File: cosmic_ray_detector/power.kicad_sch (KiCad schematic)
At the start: 16 parts, among them U2 TPS7A30, U3 TPS7A49

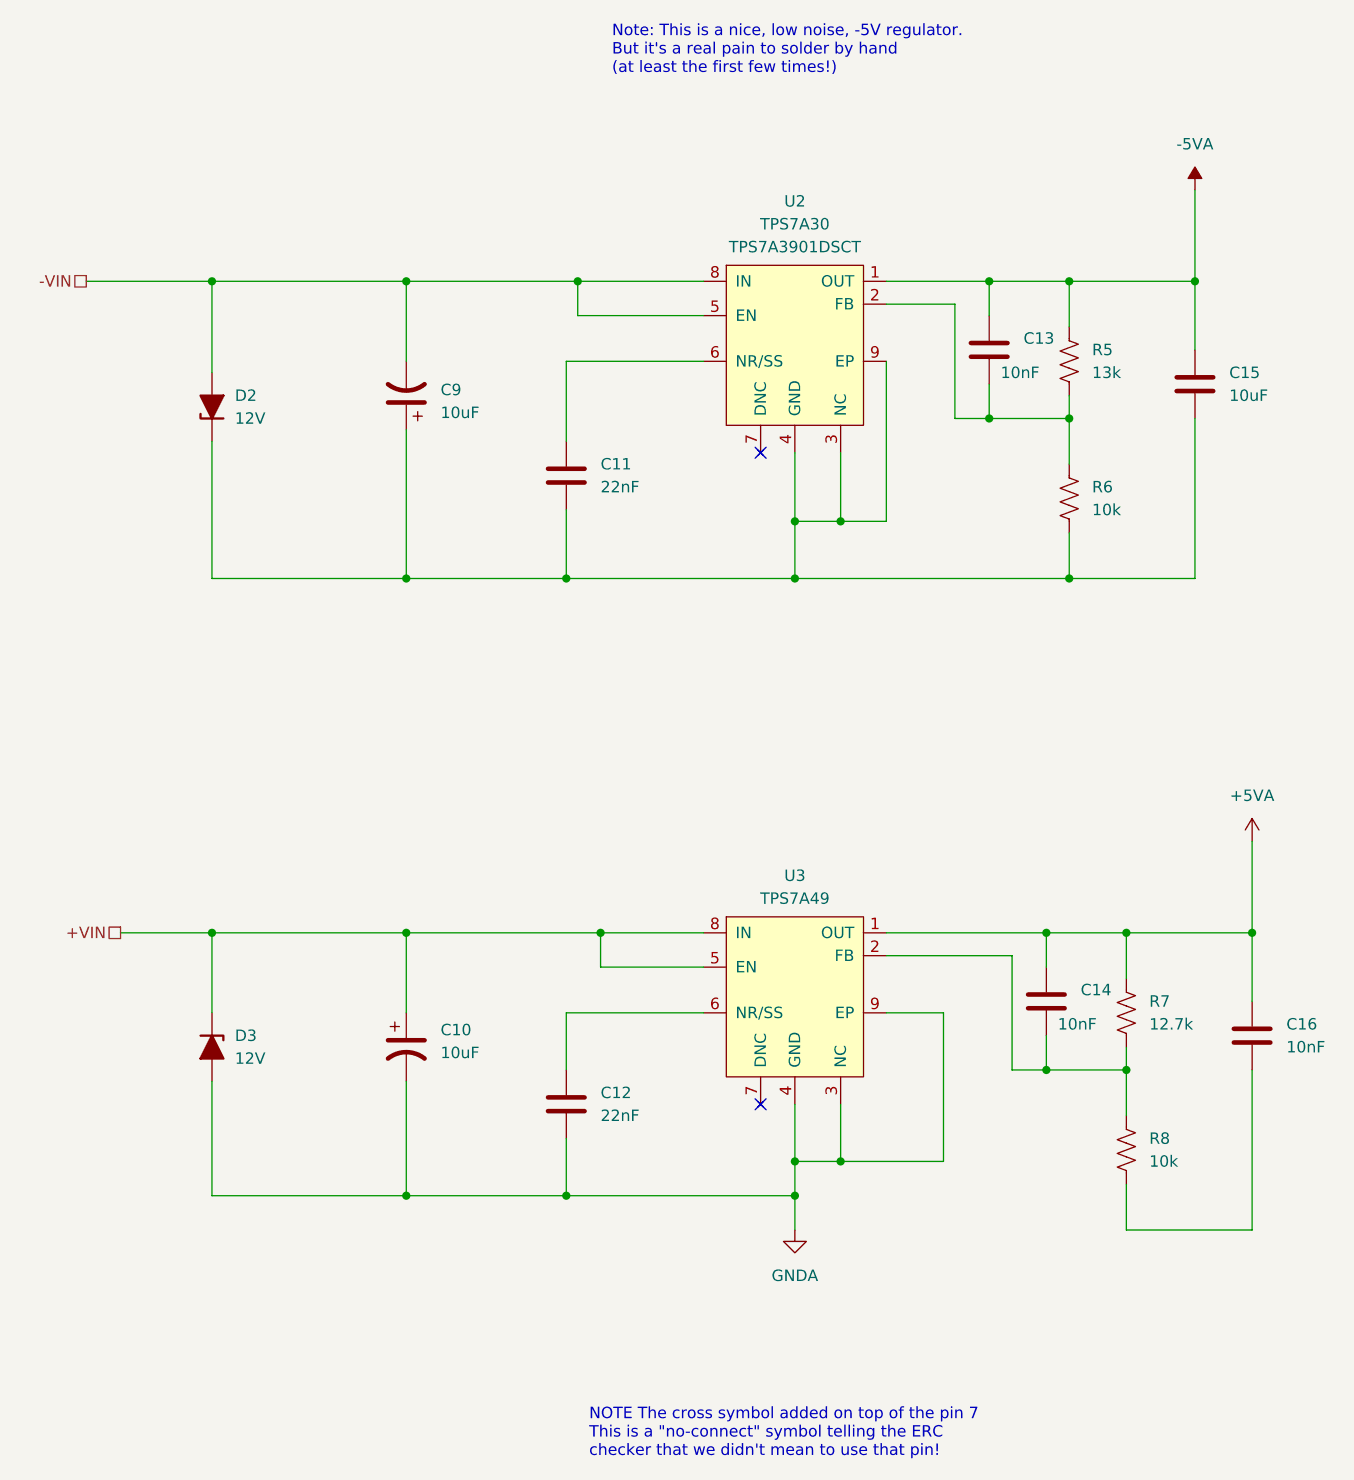
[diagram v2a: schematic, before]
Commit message: updated, now passes ERC
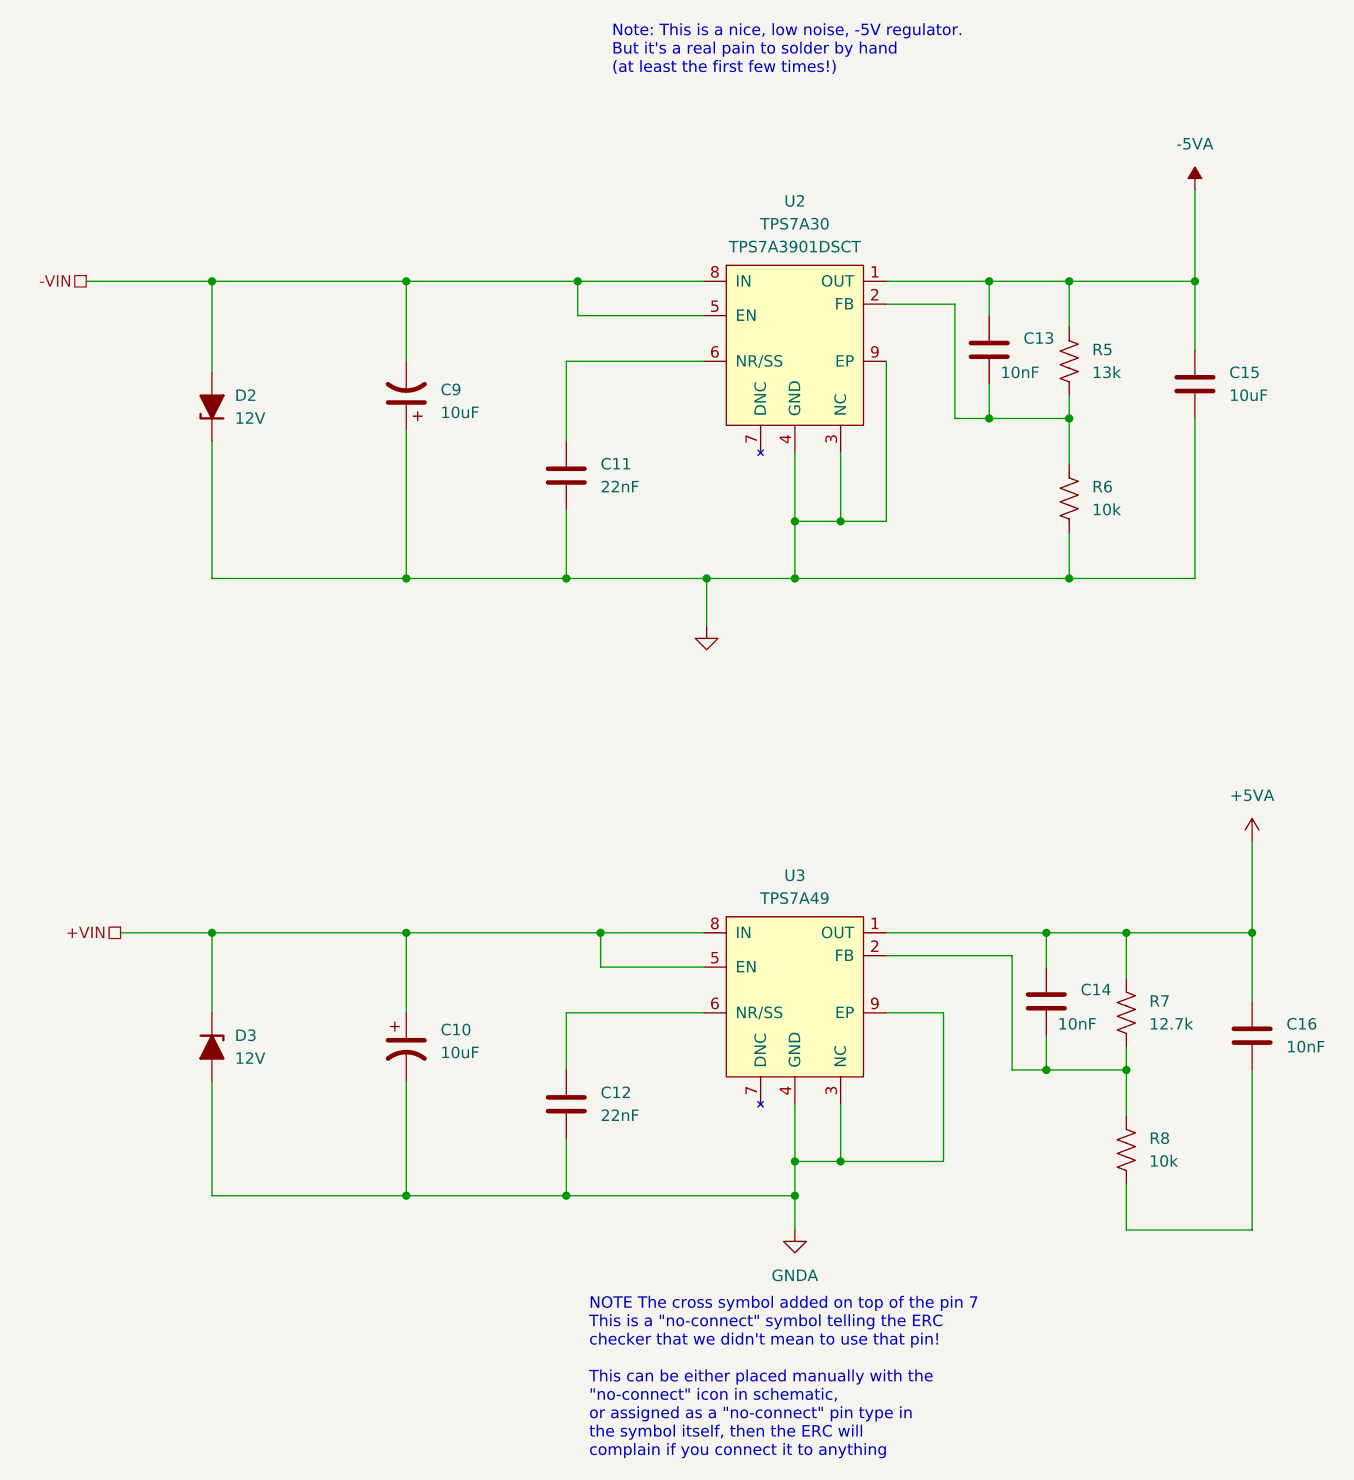
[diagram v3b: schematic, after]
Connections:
- net GNDA: now also C11.2, C15.2, C9.1, D2.1 (K), R6.2, U2.3 (NC), U2.4 (GND), U2.9 (EP)
- no-connect marks 2 -> 0
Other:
- note added: "NOTE The cross symbol added on top of the pin 7 This is a "no-connect" symbol telling the ERC checker that we didn't mean to use that pin! This can be either placed manually with the "no-connect" icon in schematic, or assigned as a "no-connect" pin type in the symbol itself, then the ERC will complain if you connect it to anything"
- note removed: "NOTE The cross symbol added on top of the pin 7 This is a "no-connect" symbol telling the ERC checker that we didn't mean to use that pin!"

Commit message: add more 3d parts symbols to library
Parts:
- U2, U3: footprint SPIRIT:MSOP-8-1EP_3x3mm_P0.65mm_EP1.73x1.85mm_ThermalVias -> (none)
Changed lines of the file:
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@@
     (property "Reference" "U2" (id 0) (at 125.73 43.18 0))
     (property "Value" "TPS7A30" (id 1) (at 125.73 45.72 0))
-    (property "Footprint" "SPIRIT:MSOP-8-1EP_3x3mm_P0.65mm_EP1.73x1.85mm_ThermalVias" (id 2) (at 125.73 54.61 0)
+    (property "Footprint" "" (id 2) (at 125.73 54.61 0)
       (effects (font (size 1.27 1.27)) hide)
     )
@@
     (property "Reference" "U3" (id 0) (at 125.73 118.11 0))
     (property "Value" "TPS7A49" (id 1) (at 125.73 120.65 0))
-    (property "Footprint" "SPIRIT:MSOP-8-1EP_3x3mm_P0.65mm_EP1.73x1.85mm_ThermalVias" (id 2) (at 125.73 127 0)
+    (property "Footprint" "" (id 2) (at 125.73 127 0)
       (effects (font (size 1.27 1.27)) hide)
     )

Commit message: many more footprints coming in
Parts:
- C10, C15, C9: value 10uF -> (none); Farnell (none) -> 1187014; MPN (none) -> MAL215375109E3; Manufacturer_Name (none) -> Vishay
- C11, C12: value 22nF -> (none)
- C13, C14, C16: value 10nF -> (none)
- D2, D3: value 12V -> (none); footprint Diode_SMD:D_SOD-123 -> (none); Manufacturer ONSEMI -> (none); Manufacturer_Name (none) -> ONSEMI
- R5: value 13k -> (none)
- R6, R8: value 10k -> (none)
- R7: value 12.7k -> (none)
- U2: value TPS7A30 -> (none); Farnell (none) -> 1855138; farnell 1855138 -> (none)
- U3: value TPS7A49 -> (none); Farnell (none) -> 1841881; farnell 1841881 -> (none)
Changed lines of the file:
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@@
       (effects (font (size 1.27 1.27)) (justify left))
     )
-    (property "Value" "10k" (id 1) (at 165.1 149.8599 0)
+    (property "Value" "" (id 1) (at 165.1 149.8599 0)
       (effects (font (size 1.27 1.27)) (justify left))
     )
@@
       (effects (font (size 1.27 1.27)) (justify left))
     )
-    (property "Value" "12.7k" (id 1) (at 165.1 134.6199 0)
+    (property "Value" "" (id 1) (at 165.1 134.6199 0)
       (effects (font (size 1.27 1.27)) (justify left))
     )
@@
       (effects (font (size 1.27 1.27)) (justify left))
     )
-    (property "Value" "10uF" (id 1) (at 86.36 137.7949 0)
+    (property "Value" "" (id 1) (at 86.36 137.7949 0)
       (effects (font (size 1.27 1.27)) (justify left))
     )
@@
       (effects (font (size 1.27 1.27)) hide)
     )
+    (property "Farnell" "1187014 " (id 4) (at 82.55 137.16 0)
+      (effects (font (size 1.27 1.27)) hide)
+    )
+    (property "MPN" "MAL215375109E3" (id 5) (at 82.55 137.16 0)
+      (effects (font (size 1.27 1.27)) hide)
+    )
+    (property "Manufacturer_Name" "Vishay" (id 6) (at 82.55 137.16 0)
+      (effects (font (size 1.27 1.27)) hide)
+    )
     (pin "1")
     (pin "2")
@@
       (effects (font (size 1.27 1.27)) (justify left))
     )
-    (property "Value" "10nF" (id 1) (at 180.34 137.1599 0)
+    (property "Value" "" (id 1) (at 180.34 137.1599 0)
       (effects (font (size 1.27 1.27)) (justify left))
     )
@@
       (effects (font (size 1.27 1.27)) (justify left))
     )
-    (property "Value" "13k" (id 1) (at 158.75 62.2299 0)
+    (property "Value" "" (id 1) (at 158.75 62.2299 0)
       (effects (font (size 1.27 1.27)) (justify left))
     )
@@
   (symbol (lib_id "power:GNDA") (at 115.9256 90.4748 0) (unit 1)
     (in_bom yes) (on_board yes) (fields_autoplaced)
-    (property "Reference" "#PWR0101" (id 0) (at 115.9256 96.8248 0)
+    (property "Reference" "#PWR012" (id 0) (at 115.9256 96.8248 0)
       (effects (font (size 1.27 1.27)) hide)
     )
@@
       (effects (font (size 1.27 1.27)) (justify left))
     )
-    (property "Value" "10k" (id 1) (at 158.75 77.4699 0)
+    (property "Value" "" (id 1) (at 158.75 77.4699 0)
       (effects (font (size 1.27 1.27)) (justify left))
     )
@@
       (effects (font (size 1.27 1.27)) (justify left))
     )
-    (property "Value" "10nF" (id 1) (at 154.94 134.62 0)
+    (property "Value" "" (id 1) (at 154.94 134.62 0)
       (effects (font (size 1.27 1.27)) (justify left))
     )
@@
   (symbol (lib_id "power:-5VA") (at 170.18 41.91 0) (unit 1)
     (in_bom yes) (on_board yes) (fields_autoplaced)
-    (property "Reference" "#PWR013" (id 0) (at 170.18 39.37 0)
+    (property "Reference" "#PWR014" (id 0) (at 170.18 39.37 0)
       (effects (font (size 1.27 1.27)) hide)
     )
@@
       (effects (font (size 1.27 1.27)) (justify left))
     )
-    (property "Value" "22nF" (id 1) (at 104.14 74.9299 0)
+    (property "Value" "" (id 1) (at 104.14 74.9299 0)
       (effects (font (size 1.27 1.27)) (justify left))
     )
@@
   (symbol (lib_id "power:GNDA") (at 125.73 157.48 0) (unit 1)
     (in_bom yes) (on_board yes) (fields_autoplaced)
-    (property "Reference" "#PWR012" (id 0) (at 125.73 163.83 0)
+    (property "Reference" "#PWR013" (id 0) (at 125.73 163.83 0)
       (effects (font (size 1.27 1.27)) hide)
     )
@@
       (effects (font (size 1.27 1.27)) (justify left))
     )
-    (property "Value" "12V" (id 1) (at 63.5 138.4299 90)
-      (effects (font (size 1.27 1.27)) (justify left))
-    )
-    (property "Footprint" "Diode_SMD:D_SOD-123" (id 2) (at 60.96 137.16 0)
+    (property "Value" "" (id 1) (at 63.5 138.4299 90)
+      (effects (font (size 1.27 1.27)) (justify left))
+    )
+    (property "Footprint" "" (id 2) (at 60.96 137.16 0)
       (effects (font (size 1.27 1.27)) hide)
     )
@@
       (effects (font (size 1.27 1.27)) hide)
     )
-    (property "Manufacturer" "ONSEMI" (id 6) (at 60.96 137.16 90)
+    (property "Manufacturer" "" (id 6) (at 60.96 137.16 90)
+      (effects (font (size 1.27 1.27)) hide)
+    )
+    (property "Manufacturer_Name" "ONSEMI" (id 7) (at 60.96 137.16 0)
       (effects (font (size 1.27 1.27)) hide)
     )
@@
     (in_bom yes) (on_board yes) (fields_autoplaced)
     (property "Reference" "U2" (id 0) (at 125.73 43.18 0))
-    (property "Value" "TPS7A30" (id 1) (at 125.73 45.72 0))
+    (property "Value" "" (id 1) (at 125.73 45.72 0))
     (property "Footprint" "" (id 2) (at 125.73 54.61 0)
       (effects (font (size 1.27 1.27)) hide)
@@
       (effects (font (size 1.27 1.27)) hide)
     )
-    (property "farnell" "1855138" (id 4) (at 125.73 43.561 0)
+    (property "farnell" "" (id 4) (at 125.73 43.561 0)
       (effects (font (size 1.27 1.27)) hide)
     )
     (property "MPN" "TPS7A3901DSCT" (id 5) (at 125.73 48.26 0))
+    (property "Farnell" "1855138" (id 6) (at 125.73 54.61 0)
+      (effects (font (size 1.27 1.27)) hide)
+    )
     (pin "1")
     (pin "2")
@@
       (effects (font (size 1.27 1.27)) (justify left))
     )
-    (property "Value" "10uF" (id 1) (at 173.99 64.7699 0)
+    (property "Value" "" (id 1) (at 173.99 64.7699 0)
       (effects (font (size 1.27 1.27)) (justify left))
     )
@@
       (effects (font (size 1.27 1.27)) hide)
     )
+    (property "Farnell" "1187014 " (id 4) (at 170.18 63.5 0)
+      (effects (font (size 1.27 1.27)) hide)
+    )
+    (property "MPN" "MAL215375109E3" (id 5) (at 170.18 63.5 0)
+      (effects (font (size 1.27 1.27)) hide)
+    )
+    (property "Manufacturer_Name" "Vishay" (id 6) (at 170.18 63.5 0)
+      (effects (font (size 1.27 1.27)) hide)
+    )
     (pin "1")
     (pin "2")
@@
     (in_bom yes) (on_board yes) (fields_autoplaced)
     (property "Reference" "U3" (id 0) (at 125.73 118.11 0))
-    (property "Value" "TPS7A49" (id 1) (at 125.73 120.65 0))
+    (property "Value" "" (id 1) (at 125.73 120.65 0))
     (property "Footprint" "" (id 2) (at 125.73 127 0)
       (effects (font (size 1.27 1.27)) hide)
@@
       (effects (font (size 1.27 1.27)) hide)
     )
-    (property "farnell" "1841881" (id 4) (at 125.73 115.951 0)
+    (property "farnell" "" (id 4) (at 125.73 115.951 0)
       (effects (font (size 1.27 1.27)) hide)
     )
     (property "MPN" "TPS7A4901DGNT" (id 5) (at 125.73 127 0)
+      (effects (font (size 1.27 1.27)) hide)
+    )
+    (property "Farnell" "1841881" (id 6) (at 125.73 127 0)
       (effects (font (size 1.27 1.27)) hide)
     )
@@
       (effects (font (size 1.27 1.27)) (justify left))
     )
-    (property "Value" "22nF" (id 1) (at 104.14 144.7799 0)
+    (property "Value" "" (id 1) (at 104.14 144.7799 0)
       (effects (font (size 1.27 1.27)) (justify left))
     )
@@
       (effects (font (size 1.27 1.27)) (justify right))
     )
-    (property "Value" "12V" (id 1) (at 63.5 67.3099 90)
+    (property "Value" "" (id 1) (at 63.5 67.3099 90)
       (effects (font (size 1.27 1.27)) (justify right))
     )
-    (property "Footprint" "Diode_SMD:D_SOD-123" (id 2) (at 60.96 66.04 0)
+    (property "Footprint" "" (id 2) (at 60.96 66.04 0)
       (effects (font (size 1.27 1.27)) hide)
     )
@@
       (effects (font (size 1.27 1.27)) hide)
     )
-    (property "Manufacturer" "ONSEMI" (id 6) (at 60.96 66.04 90)
+    (property "Manufacturer" "" (id 6) (at 60.96 66.04 90)
+      (effects (font (size 1.27 1.27)) hide)
+    )
+    (property "Manufacturer_Name" "ONSEMI" (id 7) (at 60.96 66.04 0)
       (effects (font (size 1.27 1.27)) hide)
     )
@@
       (effects (font (size 1.27 1.27)) (justify left))
     )
-    (property "Value" "10nF" (id 1) (at 148.59 62.23 0)
+    (property "Value" "" (id 1) (at 148.59 62.23 0)
       (effects (font (size 1.27 1.27)) (justify left))
     )
@@
       (effects (font (size 1.27 1.27)) (justify right))
     )
-    (property "Value" "10uF" (id 1) (at 86.36 66.6749 0)
+    (property "Value" "" (id 1) (at 86.36 66.6749 0)
       (effects (font (size 1.27 1.27)) (justify right))
     )
@@
       (effects (font (size 1.27 1.27)) hide)
     )
+    (property "Farnell" "1187014 " (id 4) (at 82.55 64.77 0)
+      (effects (font (size 1.27 1.27)) hide)
+    )
+    (property "MPN" "MAL215375109E3" (id 5) (at 82.55 64.77 0)
+      (effects (font (size 1.27 1.27)) hide)
+    )
+    (property "Manufacturer_Name" "Vishay" (id 6) (at 82.55 64.77 0)
+      (effects (font (size 1.27 1.27)) hide)
+    )
     (pin "1")
     (pin "2")
@@
   (symbol (lib_id "power:+5VA") (at 176.53 114.3 0) (unit 1)
     (in_bom yes) (on_board yes) (fields_autoplaced)
-    (property "Reference" "#PWR014" (id 0) (at 176.53 118.11 0)
-      (effects (font (size 1.27 1.27)) hide)
-    )
+    (property "Reference" "#PWR015" (id 0) (at 176.53 118.11 0)
+      (effects (font (size 1.27 1.27)) hide)
+    )

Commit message: more notes on schematic etc
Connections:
- net GNDA: no longer U2.3 (NC)
- no-connect marks 0 -> 1
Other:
- note added: "NOTE: on pin 3 above, the datasheet says "can be left open or tied to ground" I generally would prefer to tie it to ground, but illustrating the use of a "no-connect" symbol here!"
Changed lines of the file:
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@@
   (junction (at 130.81 149.86) (diameter 0) (color 0 0 0 0)
   )
-  (junction (at 130.81 78.74) (diameter 0) (color 0 0 0 0)
-  )
   (junction (at 156.21 52.07) (diameter 0) (color 0 0 0 0)
   )
@@
   (junction (at 115.9256 85.09) (diameter 0) (color 0 0 0 0)
   )
+  (no_connect (at 130.81 74.2696))
   (wire (pts (xy 162.56 124.46) (xy 162.56 129.54))
     (stroke (width 0) (type default) (color 0 0 0 0))
@@
     (stroke (width 0) (type default) (color 0 0 0 0))
   )
-  (wire (pts (xy 135.89 78.74) (xy 130.81 78.74))
+  (wire (pts (xy 125.73 78.74) (xy 135.89 78.74))
     (stroke (width 0) (type default) (color 0 0 0 0))
   )
@@
     (stroke (width 0) (type default) (color 0 0 0 0))
   )
-  (wire (pts (xy 130.81 71.12) (xy 130.81 78.74))
-    (stroke (width 0) (type default) (color 0 0 0 0))
-  )
   (wire (pts (xy 170.18 52.07) (xy 170.18 59.69))
     (stroke (width 0) (type default) (color 0 0 0 0))
@@
     (stroke (width 0) (type default) (color 0 0 0 0))
   )
+  (wire (pts (xy 130.81 71.12) (xy 130.81 74.2696))
+    (stroke (width 0) (type default) (color 0 0 0 0))
+  )
   (wire (pts (xy 162.56 157.48) (xy 176.53 157.48))
     (stroke (width 0) (type default) (color 0 0 0 0))
@@
   )
   (wire (pts (xy 115.57 133.35) (xy 100.33 133.35))
-    (stroke (width 0) (type default) (color 0 0 0 0))
-  )
-  (wire (pts (xy 130.81 78.74) (xy 125.73 78.74))
     (stroke (width 0) (type default) (color 0 0 0 0))
   )
@@
     (effects (font (size 1.27 1.27)) (justify left bottom))
   )
+  (text "NOTE: on pin 3 above, the datasheet says\n\"can be left open or tied to ground\"\n\nI generally would prefer to tie it to ground,\nbut illustrating the use of a \"no-connect\" \nsymbol here!"
+    (at 130.1496 102.108 0)
+    (effects (font (size 1.27 1.27)) (justify left bottom))
+  )
